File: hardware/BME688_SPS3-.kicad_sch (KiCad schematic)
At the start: 6 parts, among them U59 USBLC6-2P6, U6 BME688

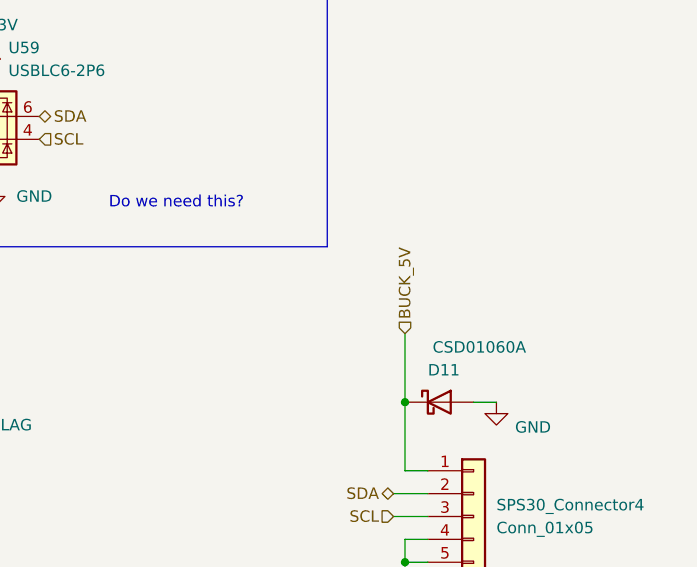
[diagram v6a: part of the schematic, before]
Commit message: updated 5V power and pin
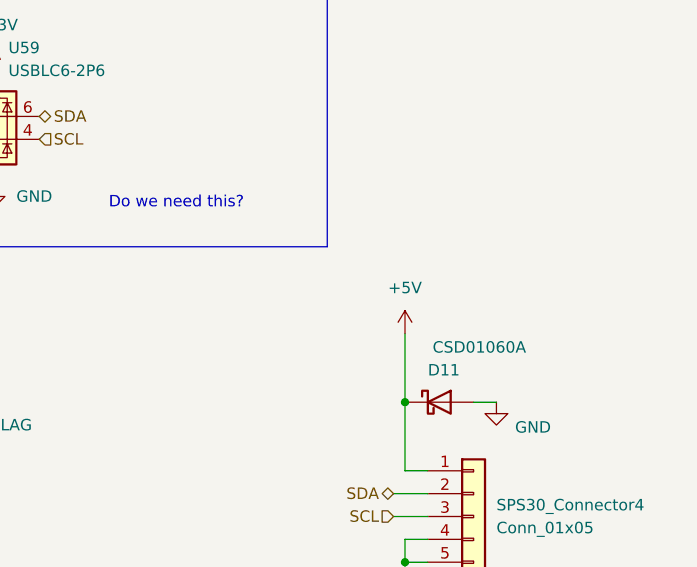
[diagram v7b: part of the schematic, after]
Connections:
- net BUCK_5V renamed +5V
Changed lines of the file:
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@@
-		)
-	)
-	(hierarchical_label "BUCK_5V"
-		(shape input)
-		(at 190.5 93.98 90)
-		(effects
-			(font
-				(size 1.27 1.27)
-			)
-			(justify left)
 		)
 	)
@@
 					(unit 1)
 				)
+			)
+		)
+	)
+	(symbol
+		(lib_id "power:+5V")
+		(at 190.5 93.98 0)
+		(unit 1)
+		(exclude_from_sim no)
+		(in_bom yes)
+		(on_board yes)
+		(dnp no)
+		(fields_autoplaced yes)
+		(property "Reference" "#PWR092"
+			(at 190.5 97.79 0)
+			(effects
+				(font
+					(size 1.27 1.27)
+				)
+				(hide yes)
+			)
+		)
+		(property "Value" "+5V"
+			(at 190.5 88.9 0)
+			(effects
+				(font
+					(size 1.27 1.27)
+				)
+			)
+		)
+		(property "Footprint" ""
+			(at 190.5 93.98 0)
+			(effects
+				(font
+					(size 1.27 1.27)
+				)
+				(hide yes)
+			)
+		)
+		(property "Datasheet" ""
+			(at 190.5 93.98 0)
+			(effects
+				(font
+					(size 1.27 1.27)
+				)
+				(hide yes)
+			)
+		)
+		(property "Description" "Power symbol creates a global label with name \"+5V\""
+			(at 190.5 93.98 0)
+			(effects
+				(font
+					(size 1.27 1.27)
+				)
+				(hide yes)
+			)
+		)
+		(pin "1"
+		)
+		(instances
+			(project "Senior_Design"
+				(path "/8f5928e8-0fc1-4443-a20f-3bfeb956761e/140ad835-eaa4-4a8c-a4e7-0525bbf22a2e"
+					(reference "#PWR092")
+					(unit 1)
+				)

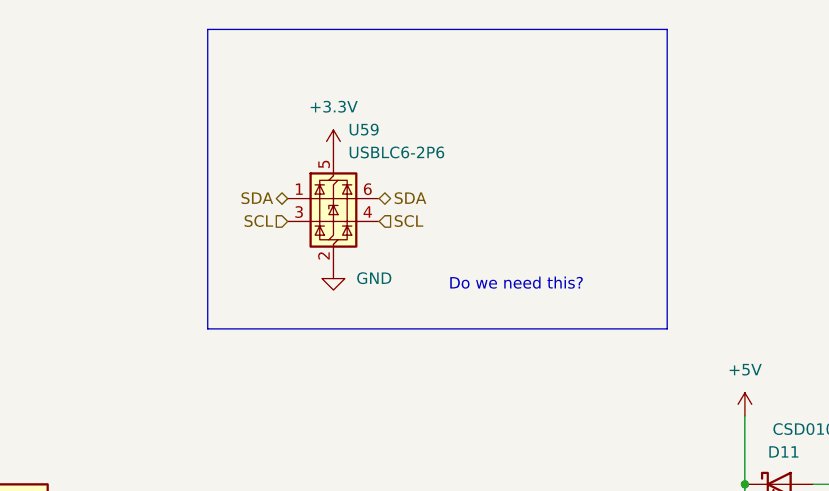
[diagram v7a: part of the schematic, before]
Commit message: passing ERC w/ exclusions
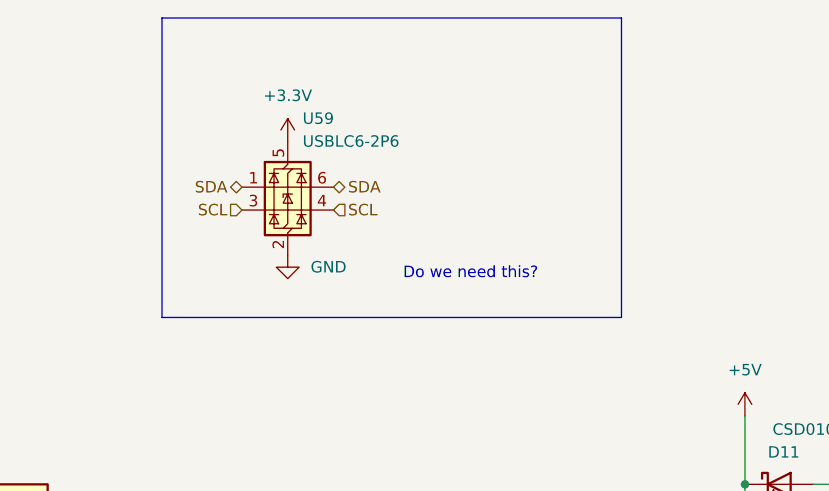
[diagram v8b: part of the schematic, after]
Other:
- moved on the sheet: U59
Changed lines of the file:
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@@
 	(paper "A4")
 	(rectangle
-		(start 130.81 51.054)
-		(end 181.864 84.328)
+		(start 125.73 49.784)
+		(end 176.784 83.058)
 		(stroke
 			(width 0)
@@
 	(text "Do we need this?"
 		(exclude_from_sim no)
-		(at 165.1 79.502 0)
+		(at 160.02 78.232 0)
 		(effects
 			(font
@@
 	(hierarchical_label "SDA"
 		(shape bidirectional)
-		(at 139.7 69.85 180)
+		(at 134.62 68.58 180)
 		(effects
 			(font
@@
 	(hierarchical_label "SCL"
 		(shape input)
-		(at 139.7 72.39 180)
+		(at 134.62 71.12 180)
 		(effects
 			(font
@@
 	(hierarchical_label "SDA"
 		(shape bidirectional)
-		(at 149.86 69.85 0)
+		(at 144.78 68.58 0)
 		(effects
 			(font
@@
 	(hierarchical_label "SCL"
 		(shape input)
-		(at 149.86 72.39 0)
+		(at 144.78 71.12 0)
 		(effects
 			(font
@@
 	(symbol
 		(lib_id "Power_Protection:USBLC6-2P6")
-		(at 144.78 69.85 0)
+		(at 139.7 68.58 0)
 		(unit 1)
 		(exclude_from_sim no)
@@
 		(fields_autoplaced yes)
 		(property "Reference" "U59"
-			(at 146.4311 62.23 0)
+			(at 141.3511 60.96 0)
 			(effects
 				(font
@@
 		)
 		(property "Value" "USBLC6-2P6"
-			(at 146.4311 64.77 0)
+			(at 141.3511 63.5 0)
 			(effects
 				(font
@@
 		)
 		(property "Footprint" "Package_TO_SOT_SMD:SOT-666"
-			(at 145.796 76.581 0)
+			(at 140.716 75.311 0)
 			(effects
 				(font
@@
 		)
 		(property "Datasheet" "https://www.st.com/resource/en/datasheet/usblc6-2.pdf"
-			(at 145.796 78.486 0)
+			(at 140.716 77.216 0)
 			(effects
 				(font
@@
 		)
 		(property "Description" "Very low capacitance ESD protection diode, 2 data-line, SOT-666"
-			(at 144.78 69.85 0)
+			(at 139.7 68.58 0)
 			(effects
 				(font
@@
 	(symbol
 		(lib_id "power:+3.3V")
-		(at 144.78 64.77 0)
+		(at 139.7 63.5 0)
 		(unit 1)
 		(exclude_from_sim no)
@@
 		(fields_autoplaced yes)
 		(property "Reference" "#PWR078"
-			(at 144.78 68.58 0)
+			(at 139.7 67.31 0)
 			(effects
 				(font
@@
 		)
 		(property "Value" "+3.3V"
-			(at 144.78 59.69 0)
+			(at 139.7 58.42 0)
 			(effects
 				(font
@@
 		)
 		(property "Footprint" ""
-			(at 144.78 64.77 0)
+			(at 139.7 63.5 0)
 			(effects
 				(font
@@
 		)
 		(property "Datasheet" ""
-			(at 144.78 64.77 0)
+			(at 139.7 63.5 0)
 			(effects
 				(font
@@
 		)
 		(property "Description" "Power symbol creates a global label with name \"+3.3V\""
-			(at 144.78 64.77 0)
+			(at 139.7 63.5 0)
 			(effects
 				(font
@@
 	(symbol
 		(lib_id "power:GND")
-		(at 144.78 77.47 0)
+		(at 139.7 76.2 0)
 		(unit 1)
 		(exclude_from_sim no)
@@
 		(fields_autoplaced yes)
 		(property "Reference" "#PWR0114"
-			(at 144.78 83.82 0)
+			(at 139.7 82.55 0)
 			(effects
 				(font
@@
 		)
 		(property "Value" "GND"
-			(at 147.32 78.7399 0)
+			(at 142.24 77.4699 0)
 			(effects
 				(font
@@
 		)
 		(property "Footprint" ""
-			(at 144.78 77.47 0)
+			(at 139.7 76.2 0)
 			(effects
 				(font
@@
 		)
 		(property "Datasheet" ""
-			(at 144.78 77.47 0)
+			(at 139.7 76.2 0)
 			(effects
 				(font
@@
 		)
 		(property "Description" "Power symbol creates a global label with name \"GND\" , ground"
-			(at 144.78 77.47 0)
-			(effects
-				(font
+			(at 139.7 76.2 0)
+			(effects
+				(font
